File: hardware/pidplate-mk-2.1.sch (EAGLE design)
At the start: 31 parts, among them Q1 2N7000, U1 ATMEGA328P, U2 MAX31855, U3 VSK-S1-3.3V

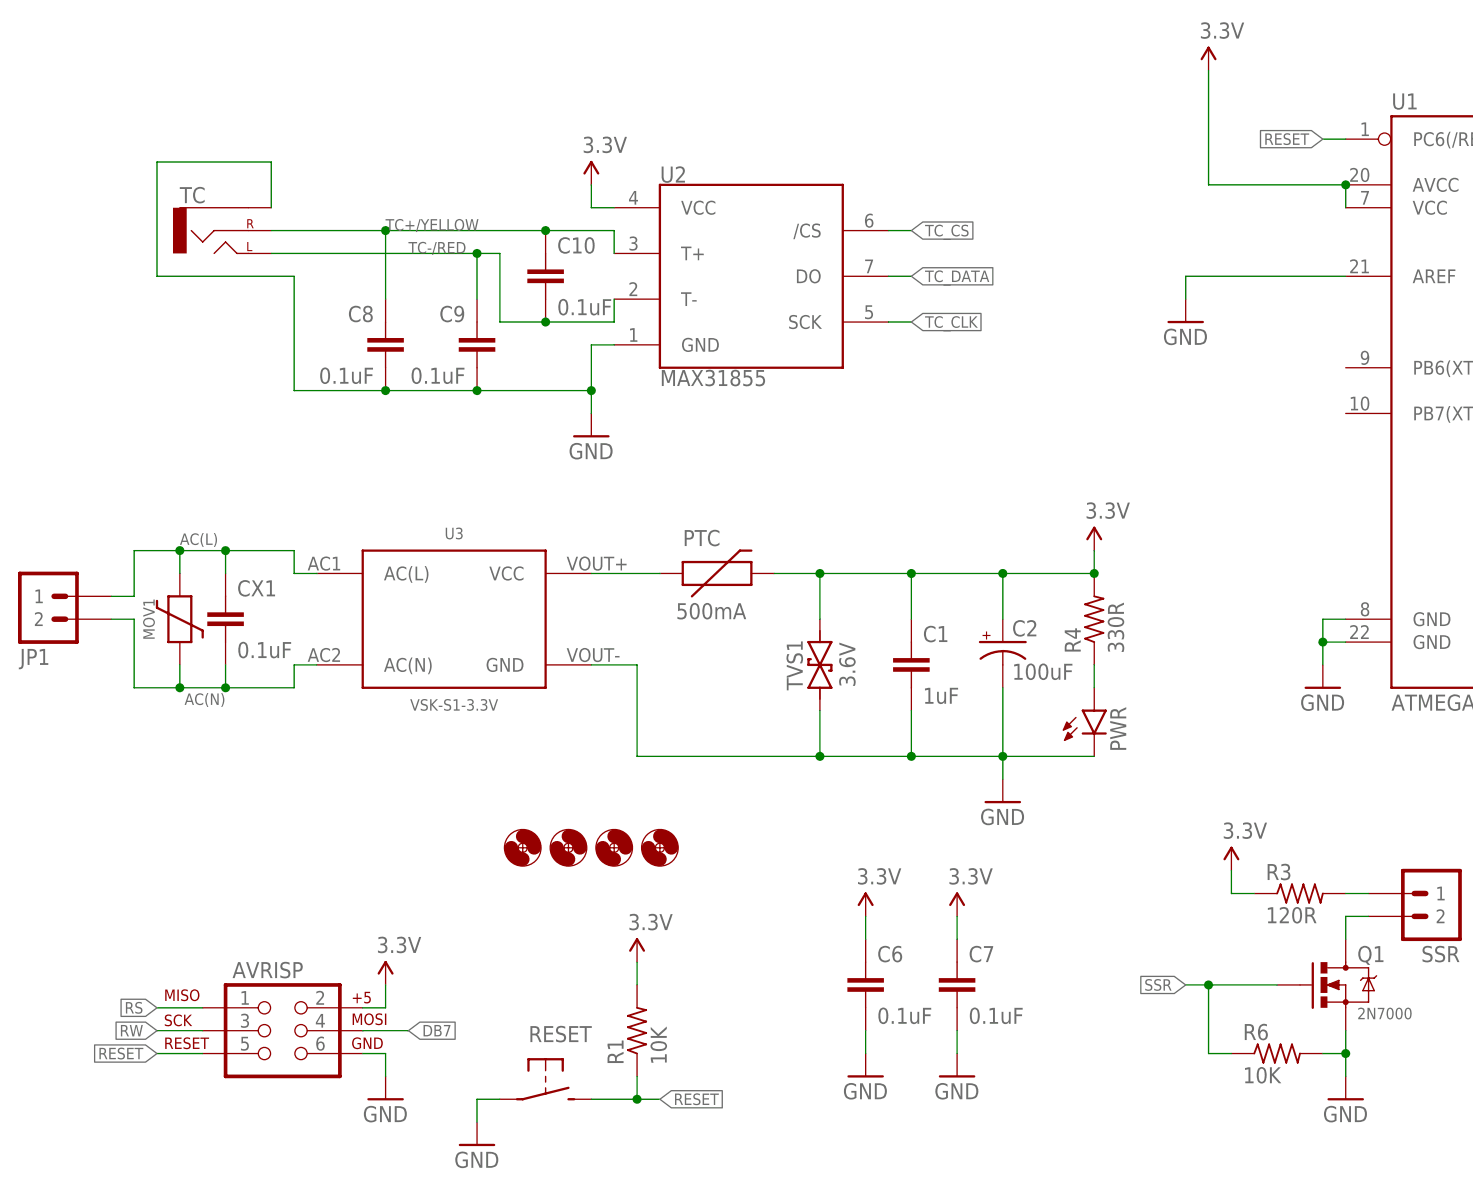
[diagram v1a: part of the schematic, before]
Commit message: now 50x50mm, reduced components, relatively happy with layout
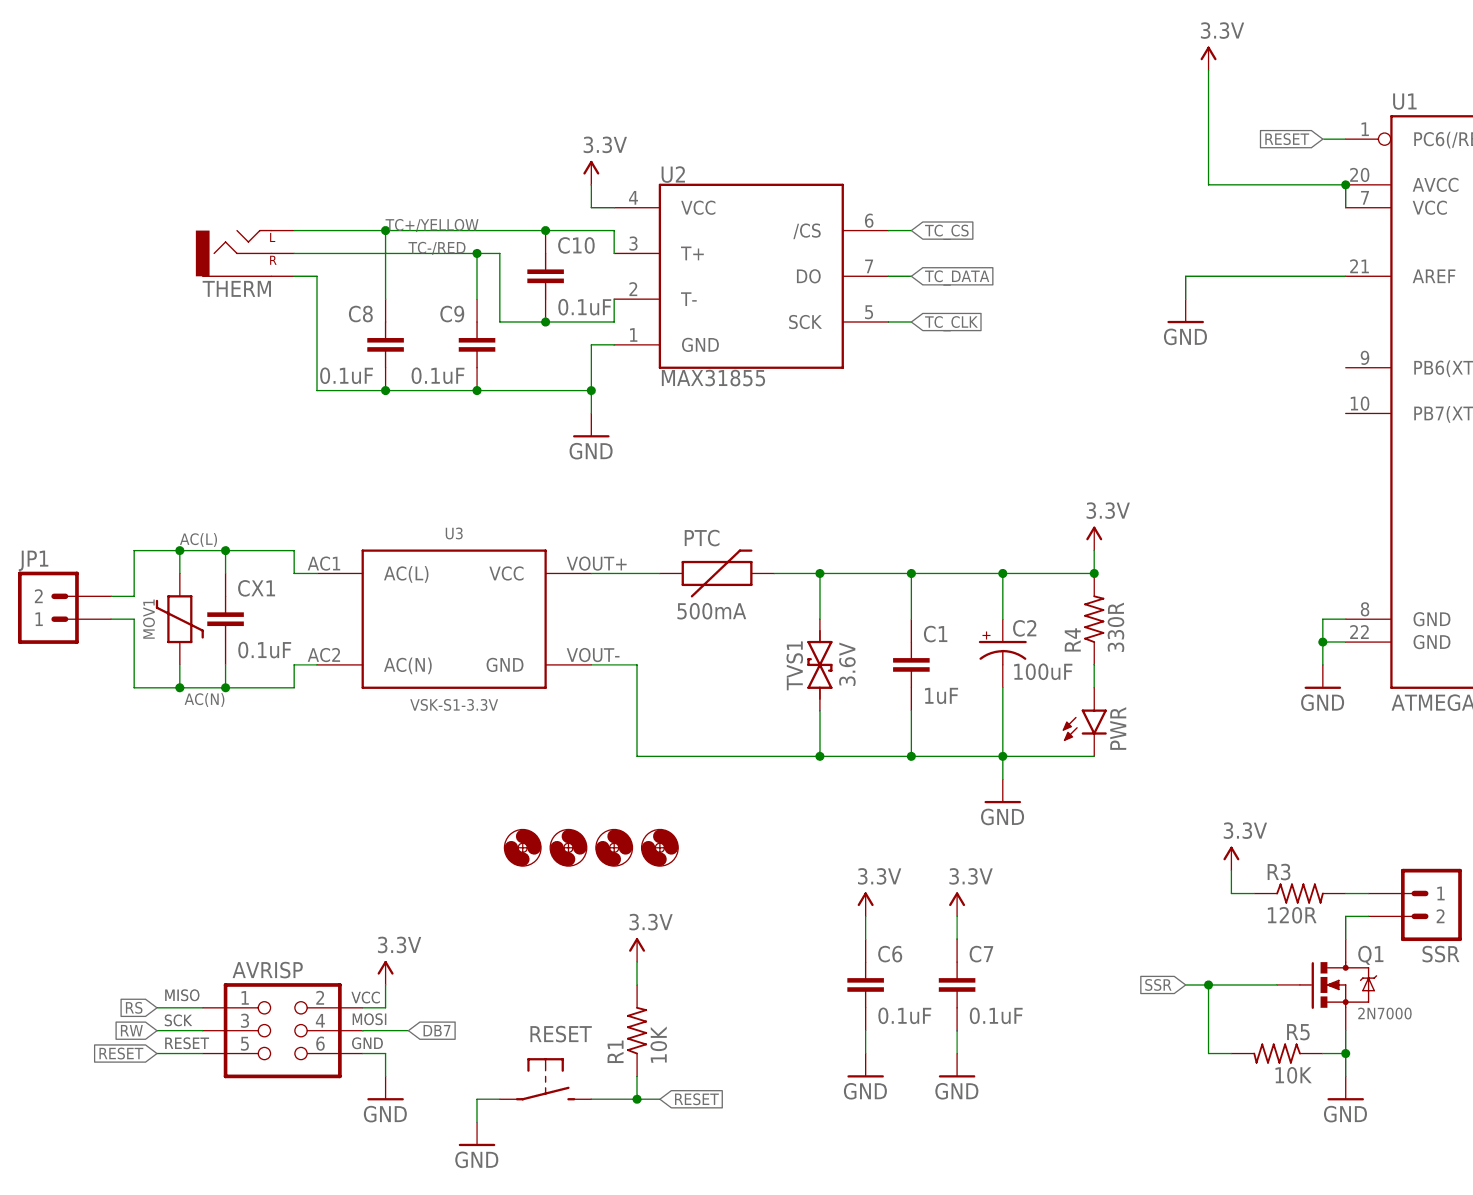
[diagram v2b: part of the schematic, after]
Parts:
- removed TC: (no value), A_butts:AUDIO-JACKPTH
- added THERM: (no value), A_butts:AUDIO-JACKPTH
- RESET: value SPST-NO-TACT3MM-PTH -> SPST-NO-TACT6MM-PTH; device A_butts:SPST-NO-TACT3MM-PTH -> A_butts:SPST-NO-TACT6MM-PTH
- renumbered R6 to R5
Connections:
- net 3.3V: now also AVRISP.VCC; no longer AVRISP.2
- net AC(L): now also JP1.2; no longer JP1.1
- net AC(N): now also JP1.1; no longer JP1.2
- net DB7: now also AVRISP.MOSI; no longer AVRISP.4
- net GND: now also AVRISP.GND, R5.1, THERM.SLEEVE; no longer AVRISP.6, R5.2, TC.SLEEVE
- net RESET: now also AVRISP.RESET; no longer AVRISP.5
- net RS: now also AVRISP.MISO; no longer AVRISP.1
- net RW: now also AVRISP.SCK; no longer AVRISP.3
- net SSR: now also R5.2; no longer R5.1
- net TC+/YELLOW: now also THERM.LEFT; no longer TC.RIGHT
- net TC-/RED: now also THERM.RIGHT; no longer TC.LEFT
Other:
- moved on the sheet: JP1
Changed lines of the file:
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@@
 <setting verticaltext="up"/>
 </settings>
-<grid distance="100" unitdist="mil" unit="mil" style="lines" multiple="1" display="yes" altdistance="1" altunitdist="mil" altunit="mil"/>
+<grid distance="100" unitdist="mil" unit="mil" style="lines" multiple="1" display="yes" altdistance="2" altunitdist="mil" altunit="mil"/>
 <layers>
 <layer number="1" name="Top" color="4" fill="1" visible="yes" active="no"/>
@@
 <part name="GND2" library="A_butts" deviceset="GND" device=""/>
 <part name="GND3" library="A_butts" deviceset="GND" device=""/>
-<part name="RESET" library="A_butts" deviceset="SPST-NO-TACT" device="3MM-PTH" value="SPST-NO-TACT3MM-PTH"/>
+<part name="RESET" library="A_butts" deviceset="SPST-NO-TACT" device="6MM-PTH" value="SPST-NO-TACT6MM-PTH"/>
 <part name="R1" library="A_butts" deviceset="RESISTOR" device="PTH-AXIAL-6.35MM" value="10K"/>
 <part name="GND4" library="A_butts" deviceset="GND" device=""/>
@@
 <part name="GND13" library="A_butts" deviceset="GND" device=""/>
 <part name="R3" library="A_butts" deviceset="RESISTOR" device="PTH-AXIAL-6.35MM" value="120R"/>
-<part name="R6" library="A_butts" deviceset="RESISTOR" device="PTH-AXIAL-6.35MM" value="10K"/>
 <part name="PWR" library="A_butts" deviceset="LED" device="3MM"/>
 <part name="R4" library="A_butts" deviceset="RESISTOR" device="PTH-AXIAL-6.35MM" value="330R"/>
@@
 <part name="MOV1" library="A_butts" deviceset="VARISITOR" device="VAR-5.08MM-PTH"/>
 <part name="CX1" library="A_butts" deviceset="CX" device="XC10B5" value="0.1uF"/>
-<part name="AVRISP" library="A_butts" deviceset="AVR_SPI_PRG_6" device="PTH"/>
+<part name="AVRISP" library="A_butts" deviceset="AVR_SPI_PRG_6" device="PTH" value="AVR_SPI_PRG_6PTH"/>
 <part name="GND16" library="A_butts" deviceset="GND" device=""/>
 <part name="JP1" library="A_butts" deviceset="M02" device="3.5MM"/>
-<part name="TC" library="A_butts" deviceset="AUDIO-JACK" device="PTH"/>
+<part name="THERM" library="A_butts" deviceset="AUDIO-JACK" device="PTH"/>
 <part name="SUPPLY7" library="A_butts" deviceset="3.3V" device=""/>
 <part name="SUPPLY9" library="A_butts" deviceset="3.3V" device=""/>
@@
 <part name="SUPPLY10" library="A_butts" deviceset="3.3V" device=""/>
 <part name="R2" library="A_butts" deviceset="RESISTOR" device="PTH-AXIAL-6.35MM" value="1k"/>
+<part name="R5" library="A_butts" deviceset="RESISTOR" device="PTH-AXIAL-6.35MM" value="10K"/>
 </parts>
 <sheets>
@@
 <instance part="GND13" gate="1" x="144.78" y="12.7"/>
 <instance part="R3" gate="G$1" x="139.7" y="35.56"/>
-<instance part="R6" gate="G$1" x="137.16" y="17.78"/>
 <instance part="PWR" gate="G$1" x="116.84" y="55.88"/>
 <instance part="R4" gate="G$1" x="116.84" y="66.04" rot="R90"/>
@@
 <instance part="AVRISP" gate="G$1" x="25.4" y="20.32"/>
 <instance part="GND16" gate="1" x="38.1" y="12.7"/>
-<instance part="JP1" gate="G$1" x="-2.54" y="71.12" rot="MR180"/>
-<instance part="TC" gate="G$1" x="20.32" y="109.22"/>
+<instance part="JP1" gate="G$1" x="-2.54" y="63.5"/>
+<instance part="THERM" gate="G$1" x="22.86" y="106.68" rot="MR180"/>
 <instance part="SUPPLY7" gate="G$1" x="129.54" y="127"/>
 <instance part="SUPPLY9" gate="G$1" x="101.6" y="33.02"/>
@@
 <instance part="SUPPLY10" gate="G$1" x="116.84" y="73.66"/>
 <instance part="R2" gate="G$1" x="180.34" y="15.24"/>
+<instance part="R5" gate="G$1" x="137.16" y="17.78" rot="MR0"/>
 </instances>
 <busses>
@@
 <wire x1="60.96" y1="91.44" x2="60.96" y2="88.9" width="0.1524" layer="91"/>
 <junction x="60.96" y="91.44"/>
-<wire x1="27.94" y1="104.14" x2="27.94" y2="91.44" width="0.1524" layer="91"/>
-<wire x1="27.94" y1="91.44" x2="38.1" y2="91.44" width="0.1524" layer="91"/>
+<wire x1="30.48" y1="104.14" x2="30.48" y2="91.44" width="0.1524" layer="91"/>
+<wire x1="30.48" y1="91.44" x2="38.1" y2="91.44" width="0.1524" layer="91"/>
 <pinref part="C8" gate="G$1" pin="2"/>
 <wire x1="38.1" y1="91.44" x2="48.26" y2="91.44" width="0.1524" layer="91"/>
@@
 <wire x1="48.26" y1="91.44" x2="60.96" y2="91.44" width="0.1524" layer="91"/>
 <junction x="48.26" y="91.44"/>
-<pinref part="TC" gate="G$1" pin="SLEEVE"/>
-<wire x1="25.4" y1="111.76" x2="25.4" y2="116.84" width="0.1524" layer="91"/>
-<wire x1="25.4" y1="116.84" x2="12.7" y2="116.84" width="0.1524" layer="91"/>
-<wire x1="12.7" y1="116.84" x2="12.7" y2="104.14" width="0.1524" layer="91"/>
-<wire x1="12.7" y1="104.14" x2="27.94" y2="104.14" width="0.1524" layer="91"/>
+<pinref part="THERM" gate="G$1" pin="SLEEVE"/>
+<wire x1="27.94" y1="104.14" x2="30.48" y2="104.14" width="0.1524" layer="91"/>
 </segment>
 <segment>
@@
 <pinref part="GND13" gate="1" pin="GND"/>
 <wire x1="144.78" y1="15.24" x2="144.78" y2="17.78" width="0.1524" layer="91"/>
-<pinref part="R6" gate="G$1" pin="2"/>
 <wire x1="144.78" y1="17.78" x2="144.78" y2="20.32" width="0.1524" layer="91"/>
 <wire x1="142.24" y1="17.78" x2="144.78" y2="17.78" width="0.1524" layer="91"/>
 <junction x="144.78" y="17.78"/>
+<pinref part="R5" gate="G$1" pin="1"/>
 </segment>
 <segment>
@@
 </segment>
 <segment>
-<pinref part="AVRISP" gate="G$1" pin="6"/>
+<pinref part="AVRISP" gate="G$1" pin="GND"/>
 <wire x1="35.56" y1="17.78" x2="38.1" y2="17.78" width="0.1524" layer="91"/>
 <wire x1="38.1" y1="17.78" x2="38.1" y2="15.24" width="0.1524" layer="91"/>
@@
 <pinref part="C10" gate="G$1" pin="2"/>
 <junction x="55.88" y="99.06"/>
-<pinref part="TC" gate="G$1" pin="LEFT"/>
-<wire x1="25.4" y1="106.68" x2="48.26" y2="106.68" width="0.1524" layer="91"/>
+<pinref part="THERM" gate="G$1" pin="RIGHT"/>
+<wire x1="27.94" y1="106.68" x2="48.26" y2="106.68" width="0.1524" layer="91"/>
 <junction x="48.26" y="106.68"/>
 </segment>
@@
 <pinref part="C10" gate="G$1" pin="1"/>
 <junction x="55.88" y="109.22"/>
-<pinref part="TC" gate="G$1" pin="RIGHT"/>
-<wire x1="38.1" y1="109.22" x2="25.4" y2="109.22" width="0.1524" layer="91"/>
+<pinref part="THERM" gate="G$1" pin="LEFT"/>
+<wire x1="27.94" y1="109.22" x2="38.1" y2="109.22" width="0.1524" layer="91"/>
 <junction x="38.1" y="109.22"/>
 </segment>
@@
 </segment>
 <segment>
-<pinref part="AVRISP" gate="G$1" pin="5"/>
+<pinref part="AVRISP" gate="G$1" pin="RESET"/>
 <wire x1="17.78" y1="17.78" x2="12.7" y2="17.78" width="0.1524" layer="91"/>
 <label x="12.7" y="17.78" size="1.27" layer="95" rot="R180" xref="yes"/>
@@
 <wire x1="137.16" y1="25.4" x2="129.54" y2="25.4" width="0.1524" layer="91"/>
 <label x="127" y="25.4" size="1.27" layer="95" rot="R180" xref="yes"/>
-<pinref part="R6" gate="G$1" pin="1"/>
 <wire x1="129.54" y1="25.4" x2="127" y2="25.4" width="0.1524" layer="91"/>
 <wire x1="132.08" y1="17.78" x2="129.54" y2="17.78" width="0.1524" layer="91"/>
 <wire x1="129.54" y1="17.78" x2="129.54" y2="25.4" width="0.1524" layer="91"/>
 <junction x="129.54" y="25.4"/>
+<pinref part="R5" gate="G$1" pin="2"/>
 </segment>
 <segment>
@@
 </segment>
 <segment>
-<pinref part="AVRISP" gate="G$1" pin="3"/>
+<pinref part="AVRISP" gate="G$1" pin="SCK"/>
 <wire x1="17.78" y1="20.32" x2="12.7" y2="20.32" width="0.1524" layer="91"/>
 <label x="12.7" y="20.32" size="1.27" layer="95" rot="R180" xref="yes"/>
@@
 </segment>
 <segment>
-<pinref part="AVRISP" gate="G$1" pin="1"/>
+<pinref part="AVRISP" gate="G$1" pin="MISO"/>
 <wire x1="17.78" y1="22.86" x2="12.7" y2="22.86" width="0.1524" layer="91"/>
 <label x="12.7" y="22.86" size="1.27" layer="95" rot="R180" xref="yes"/>
@@
 </segment>
 <segment>
-<pinref part="AVRISP" gate="G$1" pin="4"/>
+<pinref part="AVRISP" gate="G$1" pin="MOSI"/>
 <wire x1="35.56" y1="20.32" x2="40.64" y2="20.32" width="0.1524" layer="91"/>
 <label x="40.64" y="20.32" size="1.27" layer="95" xref="yes"/>
@@
 </segment>
 <segment>
-<pinref part="AVRISP" gate="G$1" pin="2"/>
+<pinref part="AVRISP" gate="G$1" pin="VCC"/>
 <wire x1="35.56" y1="22.86" x2="38.1" y2="22.86" width="0.1524" layer="91"/>
 <wire x1="38.1" y1="22.86" x2="38.1" y2="25.4" width="0.1524" layer="91"/>
@@
 <pinref part="U3" gate="G$1" pin="AC(N)"/>
 <wire x1="27.94" y1="60.96" x2="30.48" y2="60.96" width="0.1524" layer="91"/>
-<pinref part="JP1" gate="G$1" pin="2"/>
+<pinref part="JP1" gate="G$1" pin="1"/>
 <wire x1="7.62" y1="66.04" x2="10.16" y2="66.04" width="0.1524" layer="91"/>
 </segment>
@@
 <pinref part="U3" gate="G$1" pin="AC(L)"/>
 <wire x1="27.94" y1="71.12" x2="30.48" y2="71.12" width="0.1524" layer="91"/>
-<pinref part="JP1" gate="G$1" pin="1"/>
+<pinref part="JP1" gate="G$1" pin="2"/>
 <wire x1="7.62" y1="68.58" x2="10.16" y2="68.58" width="0.1524" layer="91"/>
 </segment>

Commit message: mini mini mini
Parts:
- RESET: value SPST-NO-TACT6MM-PTH -> SPST-NO-TACT3MM-PTH-SMALL-PADS; device A_butts:SPST-NO-TACT6MM-PTH -> A_butts:SPST-NO-TACT3MM-PTH-SMALL-PADS
- THERM: device A_butts:AUDIO-JACKPTH -> A_butts:AUDIO-JACK2.5MM
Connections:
- net 3.3V: now also R1.1; no longer R1.2
- net GND: now also R5.2; no longer R5.1
- net N$6: now also SSR.2; no longer SSR.1
- net N$9: now also SSR.1; no longer SSR.2
- net RESET: now also R1.2; no longer R1.1
- net SSR: now also R5.1; no longer R5.2
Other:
- moved on the sheet: SSR
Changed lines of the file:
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@@
 <part name="GND2" library="A_butts" deviceset="GND" device=""/>
 <part name="GND3" library="A_butts" deviceset="GND" device=""/>
-<part name="RESET" library="A_butts" deviceset="SPST-NO-TACT" device="6MM-PTH" value="SPST-NO-TACT6MM-PTH"/>
+<part name="RESET" library="A_butts" deviceset="SPST-NO-TACT" device="3MM-PTH-SMALL-PADS" value="SPST-NO-TACT3MM-PTH-SMALL-PADS"/>
 <part name="R1" library="A_butts" deviceset="RESISTOR" device="PTH-AXIAL-6.35MM" value="10K"/>
 <part name="GND4" library="A_butts" deviceset="GND" device=""/>
@@
 <part name="GND16" library="A_butts" deviceset="GND" device=""/>
 <part name="JP1" library="A_butts" deviceset="M02" device="3.5MM"/>
-<part name="THERM" library="A_butts" deviceset="AUDIO-JACK" device="PTH"/>
+<part name="THERM" library="A_butts" deviceset="AUDIO-JACK" device="2.5MM"/>
 <part name="SUPPLY7" library="A_butts" deviceset="3.3V" device=""/>
 <part name="SUPPLY9" library="A_butts" deviceset="3.3V" device=""/>
@@
 <instance part="GND3" gate="1" x="142.24" y="58.42"/>
 <instance part="RESET" gate="G$1" x="55.88" y="12.7"/>
-<instance part="R1" gate="G$1" x="66.04" y="20.32" rot="R90"/>
+<instance part="R1" gate="G$1" x="66.04" y="20.32" rot="MR90"/>
 <instance part="GND4" gate="1" x="48.26" y="7.62"/>
 <instance part="GND5" gate="1" x="127" y="99.06"/>
 <instance part="GND7" gate="1" x="101.6" y="15.24"/>
-<instance part="SSR" gate="G$1" x="157.48" y="38.1" rot="R180"/>
+<instance part="SSR" gate="G$1" x="157.48" y="30.48" rot="MR0"/>
 <instance part="SUPPLY4" gate="G$1" x="60.96" y="114.3"/>
 <instance part="Q1" gate="G$1" x="144.78" y="25.4"/>
@@
 <instance part="SUPPLY10" gate="G$1" x="116.84" y="73.66"/>
 <instance part="R2" gate="G$1" x="180.34" y="15.24"/>
-<instance part="R5" gate="G$1" x="137.16" y="17.78" rot="MR0"/>
+<instance part="R5" gate="G$1" x="137.16" y="17.78"/>
 </instances>
 <busses>
@@
 <wire x1="142.24" y1="17.78" x2="144.78" y2="17.78" width="0.1524" layer="91"/>
 <junction x="144.78" y="17.78"/>
-<pinref part="R5" gate="G$1" pin="1"/>
+<pinref part="R5" gate="G$1" pin="2"/>
 </segment>
 <segment>
@@
 <segment>
 <pinref part="RESET" gate="G$1" pin="2"/>
-<pinref part="R1" gate="G$1" pin="1"/>
+<pinref part="R1" gate="G$1" pin="2"/>
 <wire x1="60.96" y1="12.7" x2="66.04" y2="12.7" width="0.1524" layer="91"/>
-<wire x1="66.04" y1="12.7" x2="66.04" y2="15.24" width="0.1524" layer="91"/>
+<wire x1="66.04" y1="12.7" x2="66.04" y2="25.4" width="0.1524" layer="91"/>
 <wire x1="66.04" y1="12.7" x2="68.58" y2="12.7" width="0.1524" layer="91"/>
 <junction x="66.04" y="12.7"/>
@@
 <wire x1="129.54" y1="17.78" x2="129.54" y2="25.4" width="0.1524" layer="91"/>
 <junction x="129.54" y="25.4"/>
-<pinref part="R5" gate="G$1" pin="2"/>
+<pinref part="R5" gate="G$1" pin="1"/>
 </segment>
 <segment>
@@
 </segment>
 <segment>
-<pinref part="R1" gate="G$1" pin="2"/>
+<pinref part="R1" gate="G$1" pin="1"/>
 <pinref part="SUPPLY6" gate="G$1" pin="3.3V"/>
-<wire x1="66.04" y1="27.94" x2="66.04" y2="25.4" width="0.1524" layer="91"/>
+<wire x1="66.04" y1="27.94" x2="66.04" y2="15.24" width="0.1524" layer="91"/>
 </segment>
 <segment>
@@
 <segment>
 <pinref part="Q1" gate="G$1" pin="D"/>
-<pinref part="SSR" gate="G$1" pin="2"/>
+<pinref part="SSR" gate="G$1" pin="1"/>
 <wire x1="144.78" y1="30.48" x2="144.78" y2="33.02" width="0.1524" layer="91"/>
 <wire x1="144.78" y1="33.02" x2="147.32" y2="33.02" width="0.1524" layer="91"/>
@@
 <segment>
 <pinref part="R3" gate="G$1" pin="2"/>
-<pinref part="SSR" gate="G$1" pin="1"/>
+<pinref part="SSR" gate="G$1" pin="2"/>
 <wire x1="144.78" y1="35.56" x2="147.32" y2="35.56" width="0.1524" layer="91"/>
 </segment>
